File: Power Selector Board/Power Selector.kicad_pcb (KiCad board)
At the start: 2 copper layers, 213 x 70.8 mm, 60 parts, among them J201 64900221122, J202 64900221122, J203 64900221122, J204 MSD-DB01M-12P, J205 1998865, J206 MSD-DB01F-12P_1, J301 64900221122, J302 1998865, J303 64900221122, J304 64900221122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

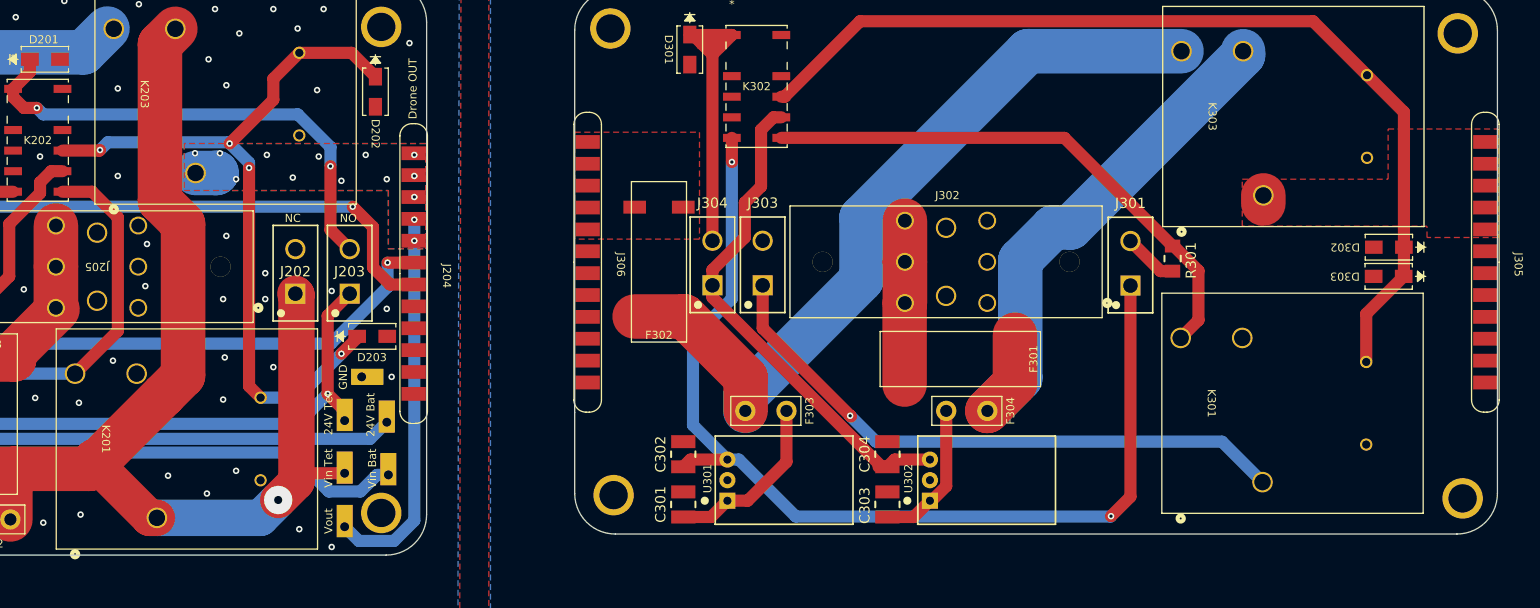
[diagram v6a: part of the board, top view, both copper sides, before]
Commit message: Fix region fills, add missing scl/sda traces & fix pad connections
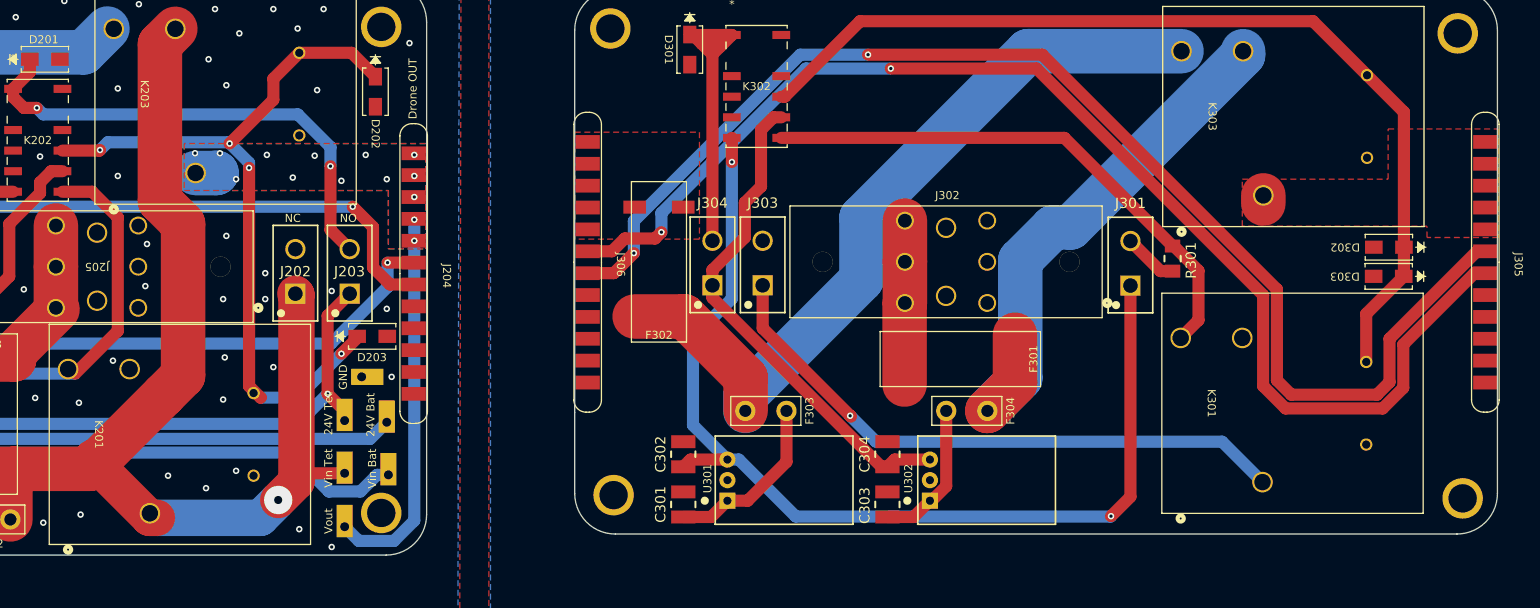
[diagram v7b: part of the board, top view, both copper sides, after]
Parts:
- moved K201 1.03 mm to (97.1, 112.4)
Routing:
- net /PCB_Droit/SCL: track 0.00 -> 158.7 mm, vias 0 -> 2
- net /PCB_Droit/SDA: track 0.00 -> 155.6 mm, vias 0 -> 2
- net 24V_Tether_D: track 63.3 -> 62.2 mm

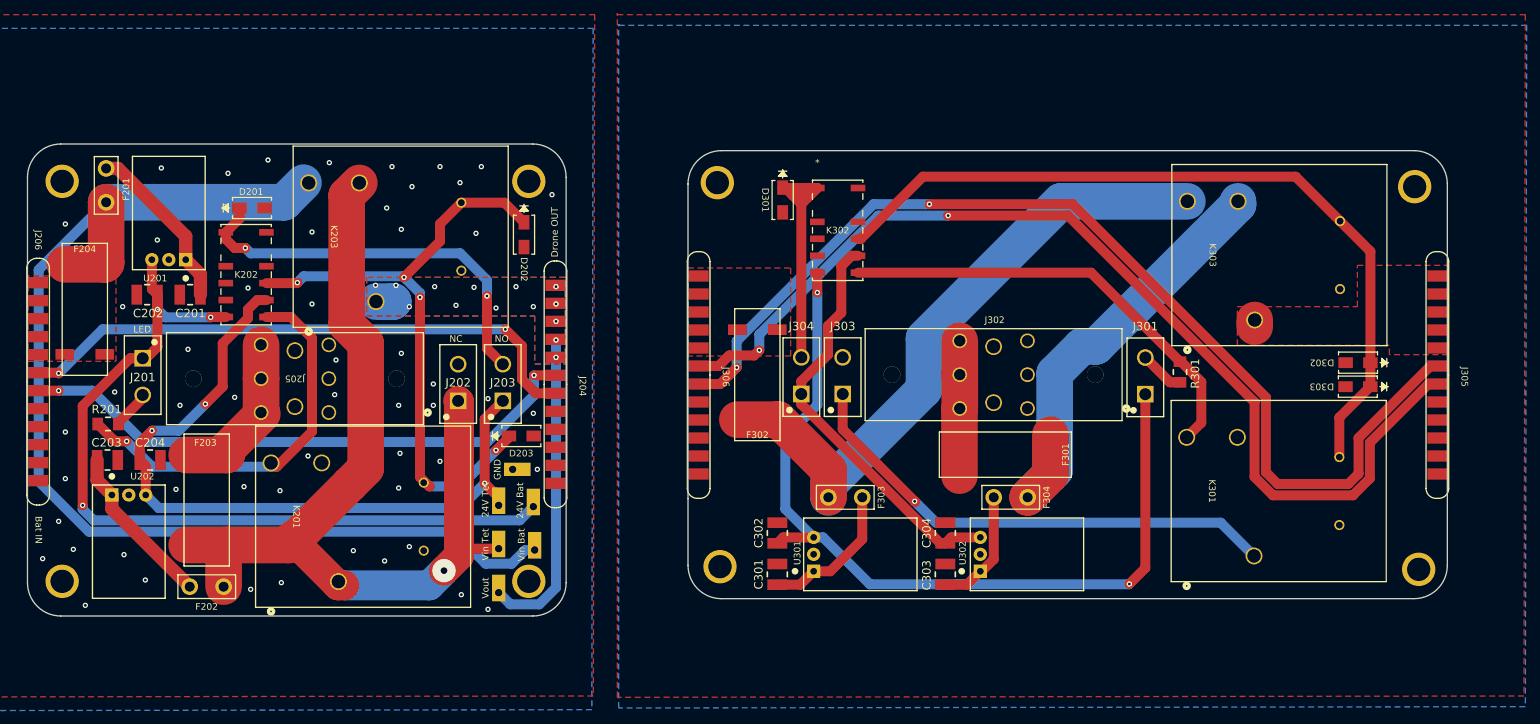
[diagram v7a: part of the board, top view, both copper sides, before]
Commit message: Modif apportées à la grosseur des trous minimum pour respecter les contraintes de fabrication de l'ÉTS. Aucune erreur de DRC, seulement des warnings de silkscreen qui overlap, not an issue.
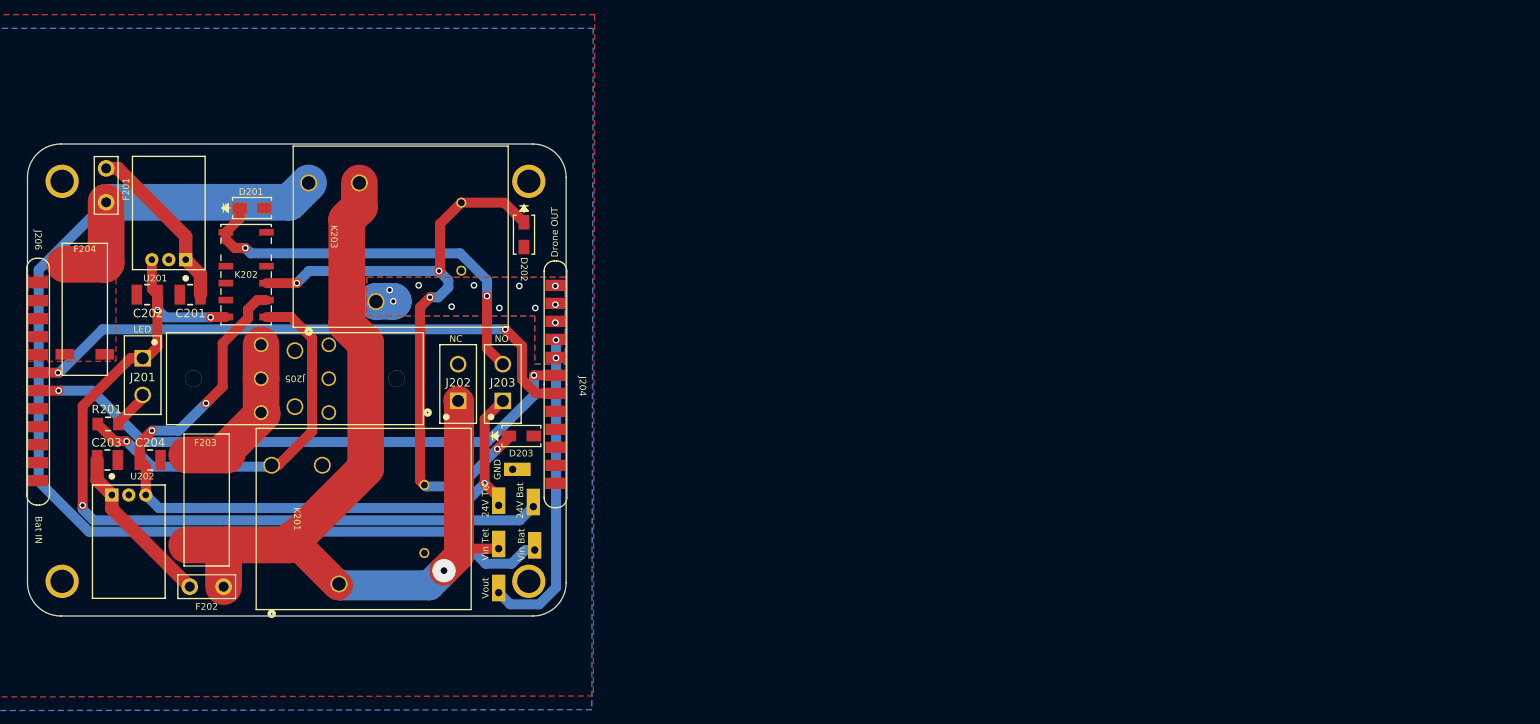
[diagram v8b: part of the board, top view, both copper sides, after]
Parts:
- removed C301, C302, C303, C304: GRM32EC72A106ME05L, Capacitors:C1210
- removed D301, D302, D303: S1D-13-F, Diodes:SMA_DIO
- removed F301, F302: 047706.3MRET1P, Fuses:3587TR
- removed F303, F304: 0698Q2000-02, Fuses:TE5_395
- removed H5, H6, H7, H8: Mounting-Hole-M3, Connectors:Mounting_Hole_3mm
- removed J301, J303, J304: 64900221122, Connectors:64900221122
- removed J302: 1998865, Connectors:1998865
- removed J305: MSD-DB01M-12P, Connectors:MSD-DB01F-12P-V2.0
- removed J306: MSD-DB01F-12P_1, Connectors:MSD-DB01F-12P-V2.0
- removed K301, K303: J115F11C24VDCSH.9, Relays:RELAY5_J115F11C24VDCSH.9_CRS
- removed K302: G6SK-2G DC24, Relays:G6SK-2G DC3_OMR
- removed R301: RC1206JR-07120RL, Resistors:R1206
- removed U301, U302: LMW78_24-0.3RL, Assembly:OKI-78SR_Horizontal
- moved K201 0.36 mm to (97.2, 112.8)
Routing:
- net /PCB_Droit/SCL: track 158.7 -> 0.00 mm, vias 2 -> 0
- net /PCB_Droit/SDA: track 155.6 -> 0.00 mm, vias 2 -> 0
- net 24V_Bat_D: track 129.0 -> 0.00 mm, vias 2 -> 0
- net /PCB_Droit/Relay_Active: track 118.1 -> 0.00 mm
- net Vin_Bat_D: track 98.7 -> 0.00 mm
- net Net-(J303-Pad1): track 75.0 -> 0.00 mm, vias 1 -> 0
- net +Vin_Tether_D: track 69.6 -> 0.00 mm
- net Net-(K301-Pad1): track 67.5 -> 0.00 mm
- net 24V_Tether_D: track 62.2 -> 0.00 mm
- net Net-(D301-Pad1): track 37.9 -> 0.00 mm
- net Net-(U301-Vin): track 21.9 -> 0.00 mm
- net Net-(F301-Pad2): track 20.1 -> 0.00 mm
- net Net-(U302-Vin): track 18.1 -> 0.00 mm
- net Net-(J301-Pad2): track 6.74 -> 0.00 mm
- net /PCB_Gauche/Relay_Active: track 94.7 -> 100.5 mm
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- removed copper zone on F.Cu, net +Vin_Drone_D
- removed copper zone on B.Cu, net GND_D
- removed copper zone on F.Cu, net GND_D
- removed copper zone on F.Cu, net Net-(F302-Pad2)
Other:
- board size 213 x 70.8 mm -> 80.8 x 70.8 mm
